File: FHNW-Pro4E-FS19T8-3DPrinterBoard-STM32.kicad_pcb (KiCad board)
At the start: 4 copper layers, 155 x 95 mm, 156 parts, among them J101 Screw_Terminal_01x02, J201 Micro_SD_Card_Det, J202 Conn_02x05_Counter_Clockwise, J203 Conn_02x05_Counter_Clockwise, J204 Conn_ARM_JTAG_SWD_10, J205 Conn_02x03_ISP, J401 Conn_01x02, J402 Conn_01x02, J403 Screw_Terminal_01x02, J404 Conn_01x02, J405 Conn_01x02, J406 Screw_Terminal_01x02, J407 Conn_01x02, J408 Conn_01x02, J409 Conn_01x02, J410 Conn_01x02, J501 Conn_01x04, J502 USB_B_Mini, J503 Conn_01x04, J601 B4B-XH-A, J602 B4B-XH-A, J603 B4B-XH-A, J604 B4B-XH-A, Q301 2N3904, Q302 2N3904, SW201 SW_Push, SW301 SW_Push, SW302 SW_Push, T401 BUK963R3-60E, T402 BUK963R3-60E, T403 BUK963R3-60E, T404 BUK963R3-60E, U101 LM2675M-3.3, U201 STM32F103ZETx, U301 ESP32-WROOM-32, U501 FT232RL, U601 TMC2660, U602 TMC2660, U603 TMC2660, U604 TMC2660, Y201 Crystal_8MHZ

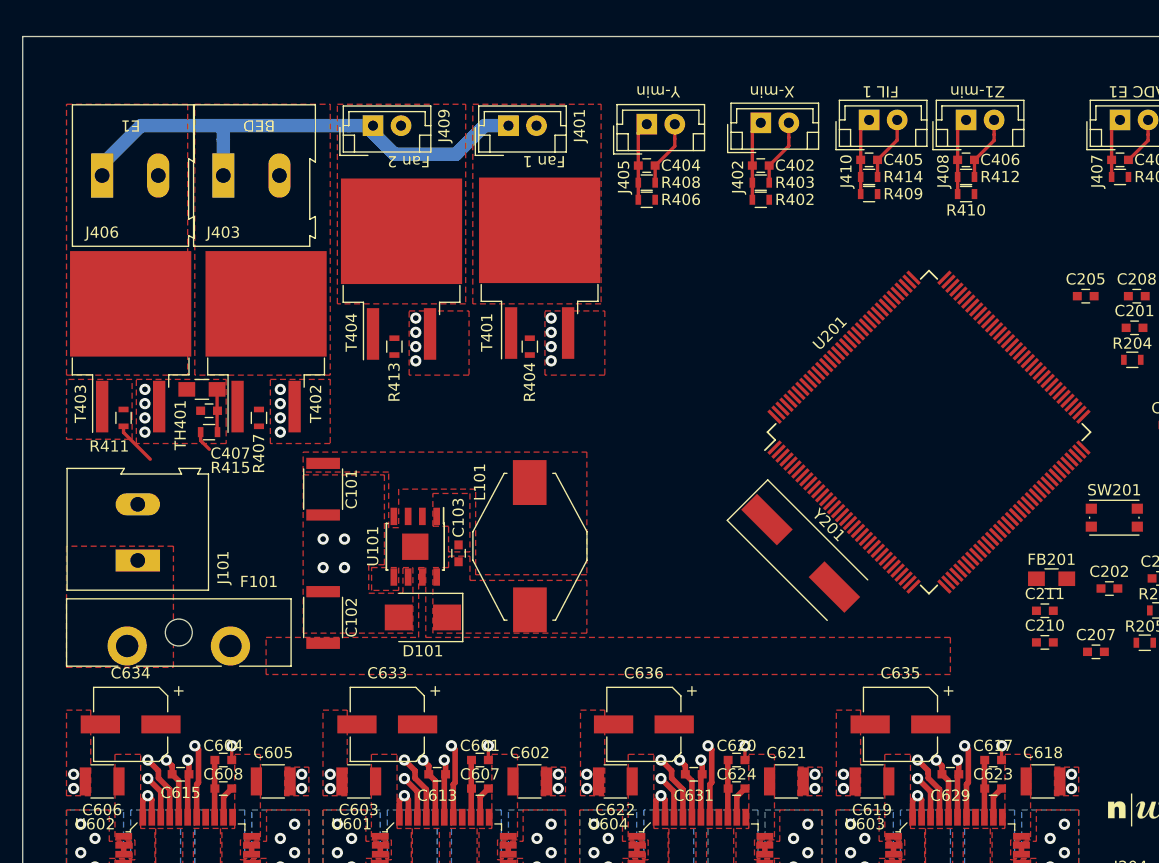
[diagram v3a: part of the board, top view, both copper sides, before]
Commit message: added LEDs
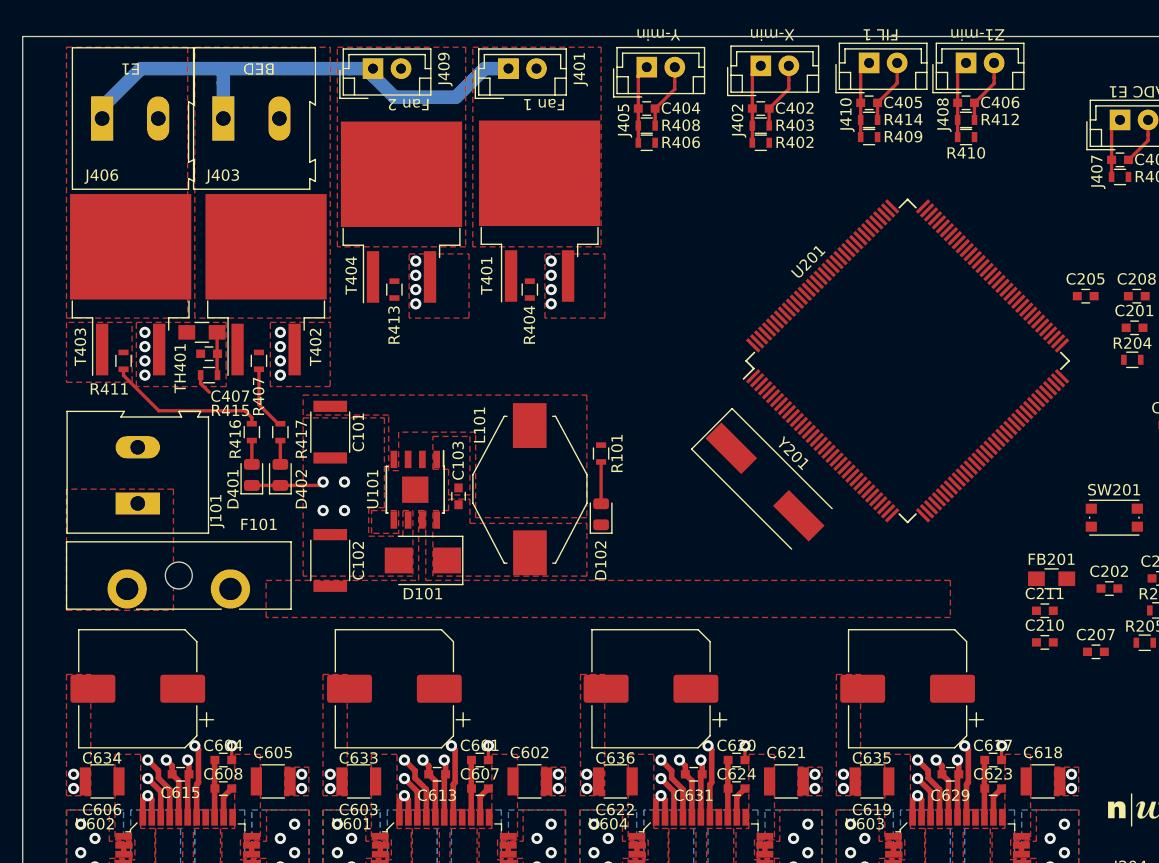
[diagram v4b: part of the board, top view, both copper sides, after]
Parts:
- added D102: LED, LED_SMD:LED_0805_2012Metric, F.Cu at (136.5, 62.6)
- added D401: LED, LED_SMD:LED_0805_2012Metric, F.Cu at (105.4, 59.1)
- added D402: LED, LED_SMD:LED_0805_2012Metric, F.Cu at (108.0, 59.1)
- added R101: 330R, Resistors_SMD:R_0603, F.Cu at (136.5, 57.1)
- added R416: 330R, Resistors_SMD:R_0603, F.Cu at (105.4, 55.2)
- added R417: 330R, Resistors_SMD:R_0603, F.Cu at (108.0, 55.2)
- C633, C634, C635, C636: footprint Capacitors_SMD:CP_Elec_6.3x5.3 -> Capacitor_SMD:CP_Elec_10x10
- moved Y201 7.10 mm to (151.1, 59.7)
- moved U201 6.63 mm to (163.8, 48.9)
- moved C101 5.12 mm to (112.4, 55.2)
- moved C102 5.12 mm to (112.4, 66.7)
- moved C103 5.08 mm to (123.8, 61.0)
- moved C407 5.08 mm to (101.6, 48.3)
- moved TH401 5.08 mm to (101.0, 46.4)
- moved J401 5.08 mm to (128.3, 22.9)
- moved J409 5.08 mm to (116.2, 22.9)
- moved R403 5.08 mm to (150.7, 27.9)
- moved R408 5.08 mm to (140.6, 27.9)
- moved R409 5.08 mm to (160.4, 29.0)
- moved R410 5.08 mm to (169.0, 29.0)
- moved R412 5.08 mm to (169.0, 27.4)
- moved R414 5.08 mm to (160.4, 27.4)
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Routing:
- net /appendix_SENSORS_POWER/DP_E1: track 3.92 -> 14.1 mm
- net GND: track 155.7 -> 162.2 mm
- net /appendix_SENSORS_POWER/DP_Bed: track 0.00 -> 5.76 mm
- net Net-(D102-Pad2): track 0.00 -> 3.73 mm
- net Net-(D402-Pad2): track 0.00 -> 2.12 mm
- net Net-(D401-Pad2): track 0.00 -> 2.12 mm

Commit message: corrected P.S. Schematic review
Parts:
- added J504: USB_C_Receptacle, Connector_USB:USB_C_Receptacle_GCT_USB4085, F.Cu at (245.1, 66.7)
- J201: footprint Connector_Card:microSD_HC_Hirose_DM3D-SF -> Connector_Card:microSD_HC_Hirose_DM3AT-SF-PEJM5
- moved C204 40.5 mm to (148.0, 45.1), turned to 45 degrees
- moved C206 33.7 mm to (171.4, 38.1), turned to 315 degrees
- moved C203 33.5 mm to (157.5, 61.0), turned to 315 degrees
- moved C202 28.1 mm to (155.6, 59.1), turned to 135 degrees
- moved C205 24.3 mm to (156.2, 36.8), turned to 45 degrees
- moved C207 22.8 mm to (179.1, 52.1), turned to 225 degrees
- moved C208 20.0 mm to (172.1, 59.1), turned to 225 degrees
- moved C209 5.61 mm to (221.6, 84.5), turned to 90 degrees
- moved J205 4.06 mm to (215.9, 82.8)
- moved J201 3.06 mm to (231.1, 82.5)
- moved Y201 2.69 mm to (153.0, 61.6)
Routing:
- net GND: track 162.2 -> 136.6 mm, vias 79 -> 76
- net +3V3: track 42.5 -> 25.9 mm, vias 5 -> 4
- net /appendix_STM32F103/D_SPI_MOSI: track 17.3 -> 6.37 mm, vias 1 -> 0
- net /appendix_STM32F103/D_SPI_SCK: track 19.8 -> 9.49 mm
- net /appendix_STM32F103/D_SPI_MISO: track 26.2 -> 17.7 mm
- net /appendix_STM32F103/SDSS: track 0.00 -> 5.07 mm
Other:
- board text removed: "SPI"

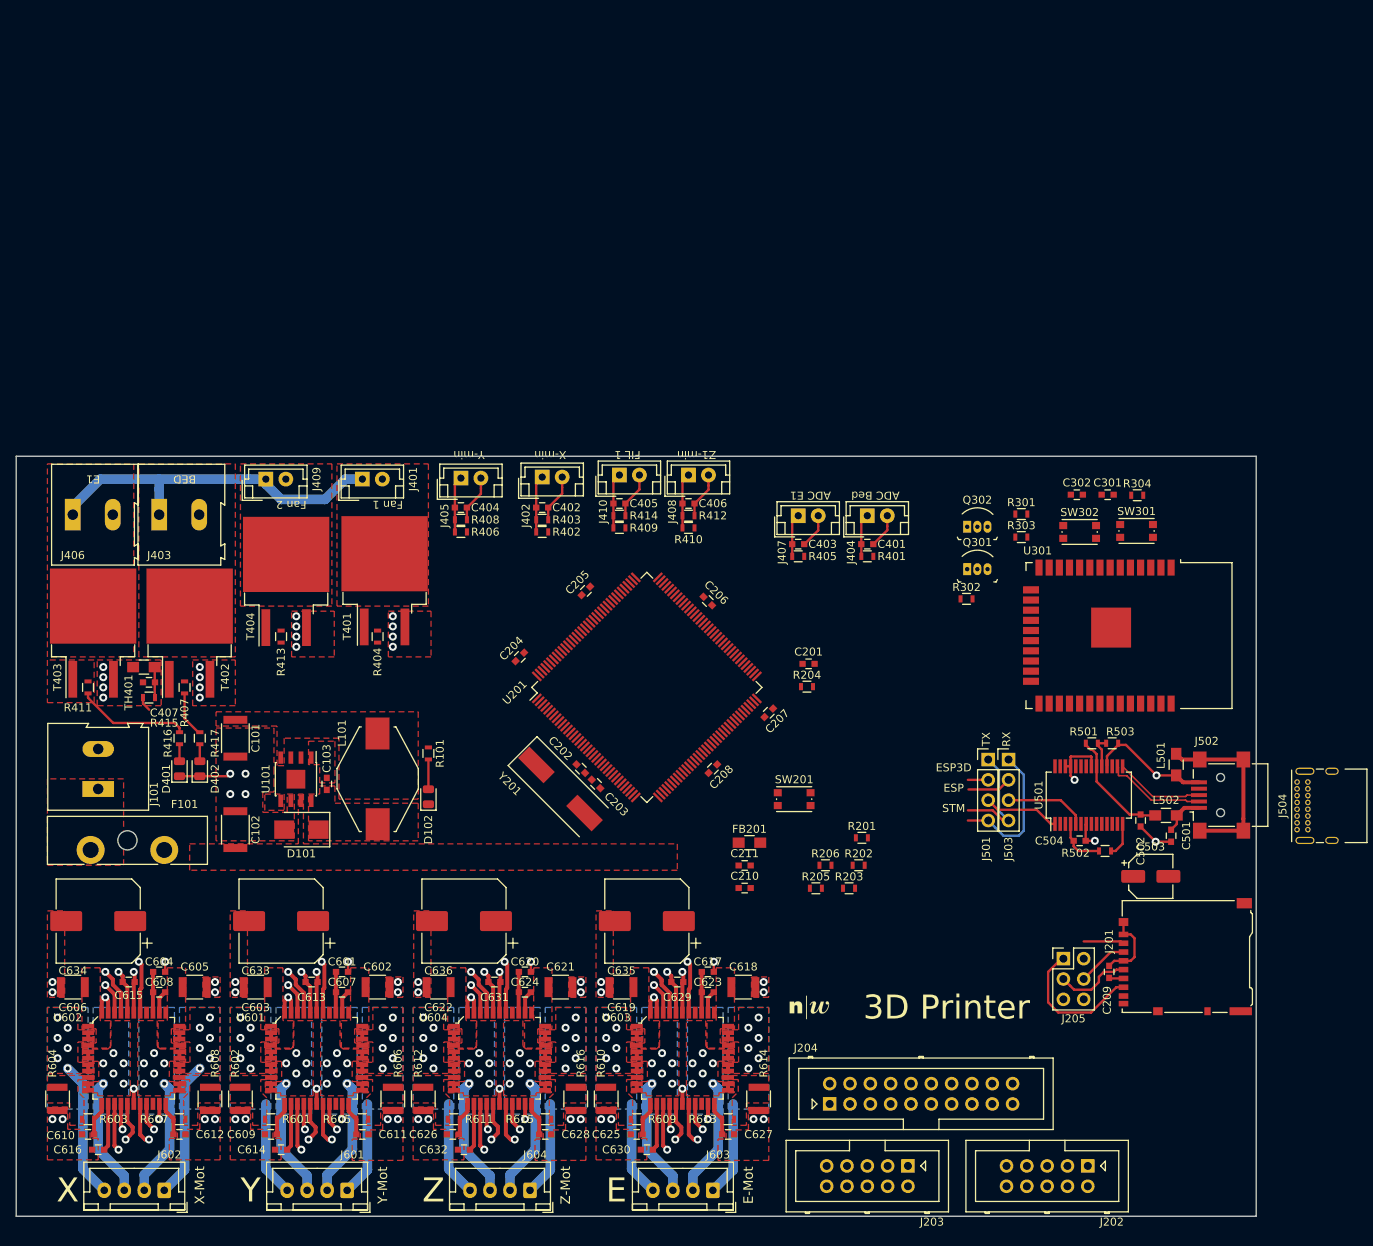
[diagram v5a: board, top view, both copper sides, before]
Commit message: added FT2232 by Marco M
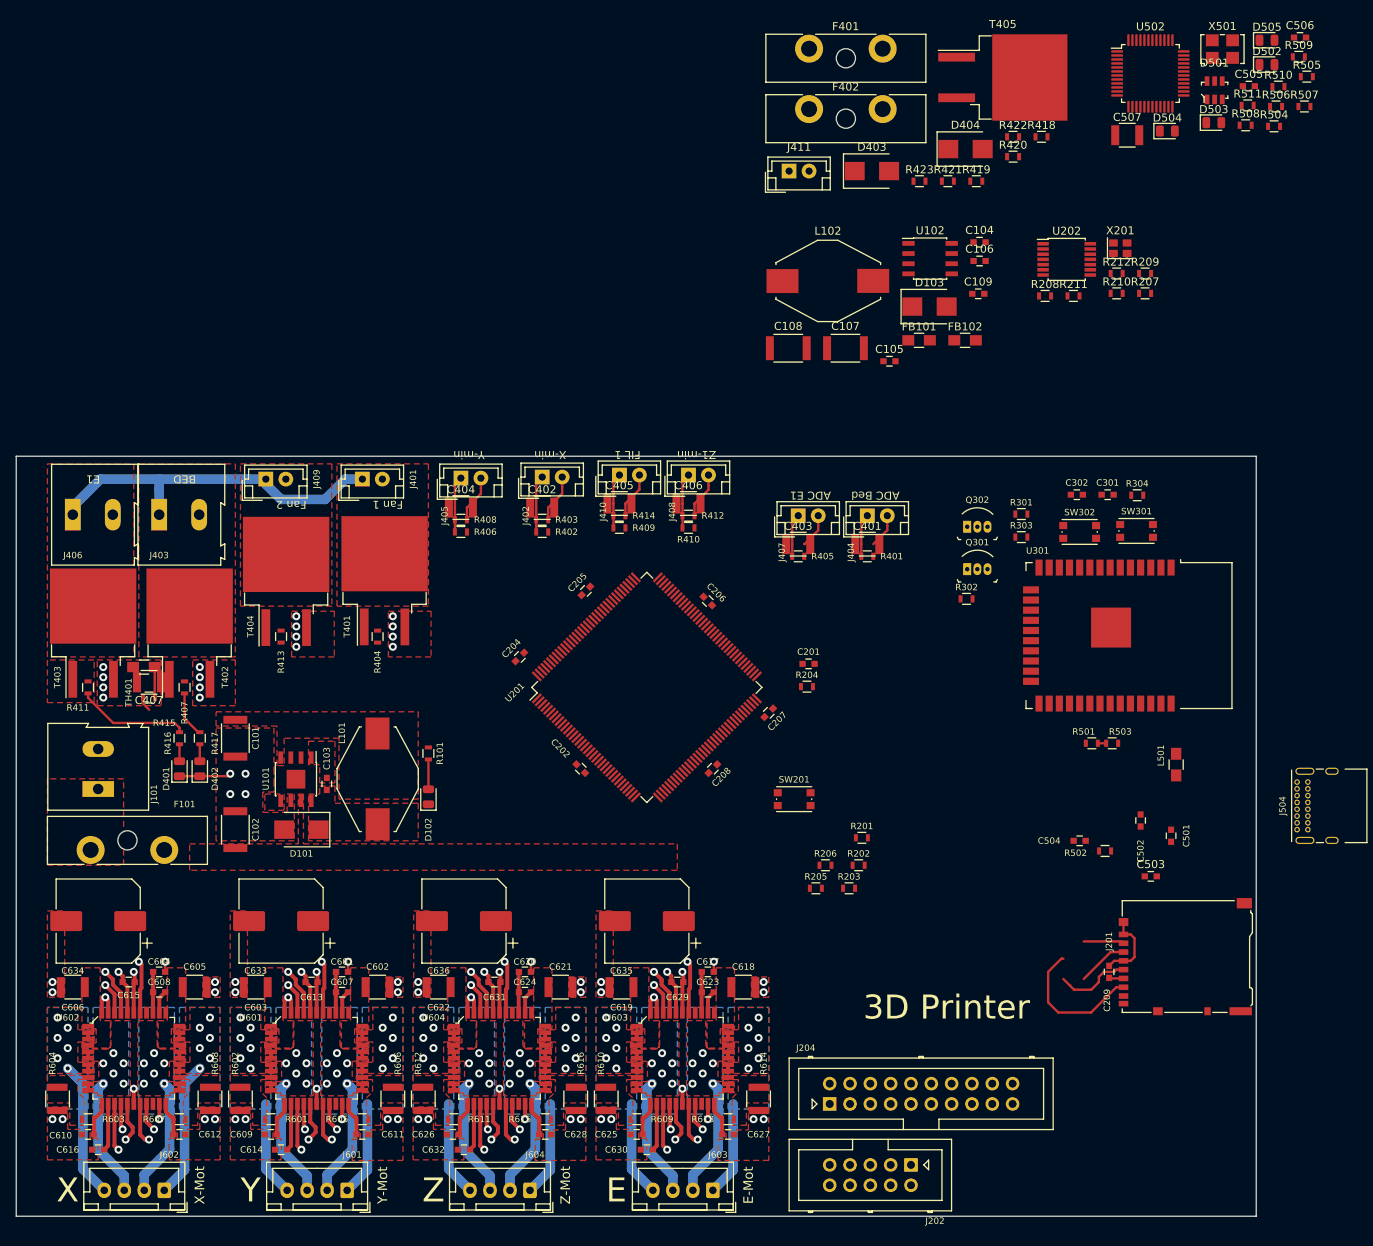
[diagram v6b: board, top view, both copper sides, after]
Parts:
- removed C203: 20p, Capacitors_SMD:C_0603
- removed C210: 10u, Capacitors_SMD:C_0603
- removed C211: 100n, Capacitors_SMD:C_0603
- removed FB201, L502: Ferrite_Bead, Resistors_SMD:R_0805_HandSoldering
- removed G***: Logo_FHNW_03x05mm, A_Tale_Of_A_Library:Logo_FHNW_03x05mm
- removed J203: Conn_02x05_Counter_Clockwise, Connector_Multicomp:Multicomp_MC9A12-1034_2x05_P2.54mm_Vertical
- removed J205: Conn_02x03_ISP, Connector_PinHeader_2.54mm:PinHeader_2x03_P2.54mm_Vertical
- removed J501, J503: Conn_01x04, Connector_PinHeader_2.54mm:PinHeader_1x04_P2.54mm_Vertical
- removed J502: USB_B_Mini, Connector_USB:USB_Mini-B_Lumberg_2486_01_Horizontal
- removed U501: FT232RL, Housings_SSOP:SSOP-28_5.3x10.2mm_Pitch0.65mm
- removed Y201: Crystal_8MHZ, Crystals:Crystal_SMD_HC49-SD
- added C104: 100n, Capacitors_SMD:C_0603, F.Cu at (205.4, -6.75)
- added C105: 100n, Capacitors_SMD:C_0603, F.Cu at (194.2, 8.13)
- added C106: 100n, Capacitors_SMD:C_0603, F.Cu at (205.4, -4.40)
- added C107: 100uF, Capacitors_SMD:C_1812, F.Cu at (188.7, 6.50)
- added C108: 330uF, Capacitors_SMD:C_1812, F.Cu at (181.5, 6.50)
- added C109: 0.01uF/50V, Capacitors_SMD:C_0603, F.Cu at (205.3, -0.30)
- added C505: 100n, Capacitors_SMD:C_0603, F.Cu at (239.1, -26.3)
- added C506: 100n, Capacitors_SMD:C_0603, F.Cu at (245.5, -32.3)
- added C507: 10u, Capacitors_SMD:C_1210, F.Cu at (223.9, -20.1)
- added D103: Shottky STPS1L30A, Diodes_SMD:D_SMB, F.Cu at (199.2, 1.30)
- added D403: Shottky STPS1L30A, Diodes_SMD:D_SMB, F.Cu at (192.0, -15.6)
- added D404: Shottky STPS1L30A, Diodes_SMD:D_SMB, F.Cu at (203.7, -18.4)
- added D501: USBLC6-2SC6, digikey-footprints:SOT23-6L, F.Cu at (234.8, -25.7)
- added D502: LED, LED_SMD:LED_0805_2012Metric, F.Cu at (241.4, -29.0)
- added D503: LED, LED_SMD:LED_0805_2012Metric, F.Cu at (234.7, -21.7)
- added D504: LED, LED_SMD:LED_0805_2012Metric, F.Cu at (228.9, -20.6)
- added D505: LED, LED_SMD:LED_0805_2012Metric, F.Cu at (241.4, -32.0)
- added F401: Fuse, Fuse:Fuseholder_Blade_ATO_Littelfuse_Pudenz_2_Pin, F.Cu at (184.1, -30.9)
- added F402: Fuse, Fuse:Fuseholder_Blade_ATO_Littelfuse_Pudenz_2_Pin, F.Cu at (184.1, -23.4)
- added FB101: Ferrite, Resistors_SMD:R_0805_HandSoldering, F.Cu at (197.9, 5.51)
- added FB102: Ferrite, Resistors_SMD:R_0805_HandSoldering, F.Cu at (203.6, 5.51)
- added J411: Conn_01x02, Connectors_JST:JST_EH_B02B-EH-A_02x2.50mm_Straight, F.Cu at (181.6, -15.6)
- added L102: 47uH DO3316-473, Inductors_SMD:L_Fastron_PISN_Handsoldering, F.Cu at (186.5, -1.90)
- added R207: 100k, Resistors_SMD:R_0603, F.Cu at (226.1, -0.36)
- added R208: 100k, Resistors_SMD:R_0603, F.Cu at (213.6, -0.04)
- added R209: 200R, Resistors_SMD:R_0603, F.Cu at (226.1, -2.84)
- added R210: 200R, Resistors_SMD:R_0603, F.Cu at (222.6, -0.36)
- added R211: 200R, Resistors_SMD:R_0603, F.Cu at (217.2, -0.04)
- added R212: 200R, Resistors_SMD:R_0603, F.Cu at (222.6, -2.84)
- added R418: 100k, Resistors_SMD:R_0603, F.Cu at (213.2, -19.9)
- added R419: 100k, Resistors_SMD:R_0603, F.Cu at (205.0, -14.4)
- added R420: 33R, Resistors_SMD:R_0603, F.Cu at (209.6, -17.4)
- added R421: 100k, Resistors_SMD:R_0603, F.Cu at (201.5, -14.4)
- added R422: 100k, Resistors_SMD:R_0603, F.Cu at (209.6, -19.9)
- added R423: 100k, Resistors_SMD:R_0603, F.Cu at (197.9, -14.4)
- added R504: 27R, Resistors_SMD:R_0603, F.Cu at (242.2, -21.2)
- added R505: 27R, Resistors_SMD:R_0603, F.Cu at (246.3, -27.4)
- added R506: 10k, Resistors_SMD:R_0603, F.Cu at (242.5, -23.7)
- added R507: 10k, Resistors_SMD:R_0603, F.Cu at (246.0, -23.7)
- added R508: 330R, Resistors_SMD:R_0603, F.Cu at (238.7, -21.4)
- added R509: 330R, Resistors_SMD:R_0603, F.Cu at (245.3, -29.9)
- added R510: 330R, Resistors_SMD:R_0603, F.Cu at (242.8, -26.2)
- added R511: 330R, Resistors_SMD:R_0603, F.Cu at (238.9, -23.8)
- added T405: BUK963R3-60E, Package_TO_SOT_SMD:TO-263-2, F.Cu at (208.3, -27.3)
- added U102: LM2675M-5, Package_SO:SOIC-8_3.9x4.9mm_P1.27mm, F.Cu at (199.2, -4.70)
- added U202: NTS0104PW-Q100J, Housings_SSOP:TSSOP-14_4.4x5mm_Pitch0.65mm, F.Cu at (216.3, -4.60)
- added U502: FT2232D, Package_QFP:LQFP-48_7x7mm_P0.5mm, F.Cu at (226.8, -27.8)
- added X201: SG-210STF, Oscillator:Oscillator_SMD_SeikoEpson_SG210-4Pin_2.5x2.0mm, F.Cu at (223.0, -6.00)
- added X501: SG5032CCN-6.000000M-HJGA3, Oscillator:Oscillator_SMD_SeikoEpson_SG8002LB-4Pin_5.0x3.2mm, F.Cu at (235.8, -30.9)
- C202: value 20p -> 10n
- C401, C402, C403, C404, C405, C406, C407: footprint Capacitors_SMD:C_0603 -> Capacitors_SMD:C_1210
- C501: value 10n -> 100n
- C503: value 4.7u -> 10n; footprint Capacitor_SMD:CP_Elec_5x5.9 -> Capacitors_SMD:C_0603
- J202: value Conn_02x05_Counter_Clockwise -> Conn_02x05_Odd_Even
- L501: value Ferrite_Bead -> WE-744232090
- R202: value 10k -> 100k
- R404, R413: value 10k -> 33R
- R501: value 4k7 -> 470R
- R502: value 10k -> 1k5
- R503: value 10k -> 4k7
- moved J202 22.1 mm to (196.8, 108.6)
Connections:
- net /appendix_ESP32/D_RX_to_ESP_TX renamed /appendix_ESP32/TX_ESP_to_RX_FTDI
- net /appendix_ESP32/D_TX_to_ESP_RX renamed /appendix_ESP32/RX_ESP_to_TX_FTDI
- net /appendix_STM32F103/SDSS renamed Net-(J201-Pad2)
- net Net-(J202-Pad1) renamed D_LCD_Beeper
- net Net-(J202-Pad2) renamed D_LCD_Encoder_BTN
- net Net-(J202-Pad3) renamed D_LCD_Encoder_B
- net Net-(J202-Pad4) renamed D_LCD_Reset
- net Net-(J202-Pad5) renamed D_LCD_Encoder_A
- C202 pad 1: Net-(C202-Pad1) -> +3V3
- C501 pad 1: Net-(C501-Pad1) -> GND
- C501 pad 2: GND -> Net-(C501-Pad2)
- C502 pad 1: V_USB -> VBUS
- C503 pad 1: V_USB -> 5V
- C504 pad 1: /appendix_UART_USB/USB_VCCIO_3.3V -> 3.3V
- J201 pad 1: GND -> Net-(J201-Pad1)
- J201 pad 3: /appendix_STM32F103/D_SPI_MOSI -> Net-(J201-Pad3)
- J201 pad 5: /appendix_STM32F103/D_SPI_SCK -> Net-(J201-Pad5)
- J201 pad 7: /appendix_STM32F103/D_SPI_MISO -> Net-(J201-Pad7)
- J202 pad 10: Net-(J202-Pad10) -> 5V
- J202 pad 6: Net-(J202-Pad6) -> Conn_LCD_SCK
- J202 pad 7: Net-(J202-Pad7) -> Conn_LCD_CS
- J202 pad 8: Net-(J202-Pad8) -> Conn_LCD_MOSI
- J202 pad 9: Net-(J202-Pad9) -> GND
- J204 pad 2: JTAG_TMS_SWDIO -> Net-(J204-Pad2)
- J204 pad 4: JTAG_TCK_SWCLK -> Net-(J204-Pad4)
- J204 pad 6: JTAG_TDO_SWO -> Net-(J204-Pad6)
- J204 pad 8: JTAG_TDI -> Net-(J204-Pad8)
- J403 pad 1: +24V -> Net-(F402-Pad1)
- J406 pad 1: +24V -> Net-(F401-Pad1)
- J504 pad A4: Net-(J504-PadA4) -> VBUS
- J504 pad A9: Net-(J504-PadA4) -> VBUS
- J504 pad B4: Net-(J504-PadA4) -> VBUS
- J504 pad B9: Net-(J504-PadA4) -> VBUS
- J504 pad S1: Net-(J504-PadS1) -> GND
- L501 pad 1: Net-(J502-Pad6) -> /appendix_UART_USB/USB_TVS_D_P
- L501 pad 2: GND -> /appendix_UART_USB/USB_SUP_D_P
- R202 pad 1: JTAG_TRST -> Net-(R202-Pad1)
- R202 pad 2: +3V3 -> Net-(R202-Pad2)
- R203 pad 1: JTAG_TMS_SWDIO -> Net-(J204-Pad2)
- R204 pad 1: JTAG_TDI -> Net-(J204-Pad8)
- R205 pad 2: JTAG_TCK_SWCLK -> Net-(J204-Pad4)
- R206 pad 2: JTAG_TDO_SWO -> Net-(J204-Pad6)
- R501 pad 1: V_USB -> Net-(C501-Pad2)
- R501 pad 2: Net-(R501-Pad2) -> 5V
- R502 pad 1: /appendix_UART_USB/USB_VCCIO_3.3V -> Net-(R502-Pad1)
- R502 pad 2: Net-(R502-Pad2) -> /appendix_UART_USB/USB_FT_D_P
- R503 pad 1: Net-(R501-Pad2) -> Net-(R503-Pad1)
- R503 pad 2: GND -> VBUS
- U101 pad 5: Net-(U101-Pad5) -> +24V
- U201 pad 23: Net-(C202-Pad1) -> /appendix_STM32F103/RCC_OSC_IN
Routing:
- net GND: track 136.6 -> 105.6 mm, vias 76 -> 72
- net Net-(J502-Pad6): track 23.0 -> 0.00 mm
- net /appendix_UART_USB/D_TX_to_STM_RX: track 17.7 -> 0.00 mm
- net Net-(J201-Pad7): track 0.00 -> 17.7 mm
- net /appendix_STM32F103/D_SPI_MISO: track 17.7 -> 0.00 mm
- net V_USB: track 14.5 -> 0.00 mm
- net /appendix_UART_USB/D_RX_to_STM_TX: track 14.3 -> 0.00 mm
- net /appendix_UART_USB/USB_D_N: track 12.6 -> 0.00 mm
- net /appendix_UART_USB/USB_D_P: track 11.2 -> 0.00 mm
- net D_TX_to_USB_RX: track 10.3 -> 0.00 mm
- net D_RX_to_USB_TX: track 9.58 -> 0.00 mm
- net Net-(J201-Pad5): track 0.00 -> 9.49 mm
- net /appendix_STM32F103/D_SPI_SCK: track 9.49 -> 0.00 mm
- net Net-(J201-Pad3): track 0.00 -> 6.37 mm
- net /appendix_STM32F103/D_SPI_MOSI: track 6.37 -> 0.00 mm
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- removed copper zone on F.Cu, net Net-(U101-Pad5)
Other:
- board text removed: "ESP"
- board text removed: "ESP3D"
- board text removed: "RX"
- board text removed: "STM"
- board text removed: "TX"
